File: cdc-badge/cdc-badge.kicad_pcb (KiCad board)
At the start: 4 copper layers, 85 x 110 mm, 158 parts, among them J1 USB_C, J2 JST S2B-PH-SM4-TB, J3 Conn_02x20_Odd_Even, J4 Conn_Grove, J5 Conn_02x03_Odd_Even, J6 Conn_01x06, J7 Conn_01x24, Q1 Si1308EDL, Q2 Si1308EDL, SW0 0, SW1 1, SW10 YES, SW11 NO, SW12 power on/reset, SW13 reset, SW14 flash/power off, SW15 MST-22D18G2 3J, SW16 MST-22D18G2 3J, SW2 2, SW3 3, SW4 4, SW5 5, SW6 6, SW7 7, SW8 8, SW9 9, U1 ESP32-S3-WROOM-1-N16R8, U2 TCA9535PWR, U3 TR01-C2P-T301, U5 TLV61070ADBVR, U6 BQ25895RTW, U8 TLV62569DBV

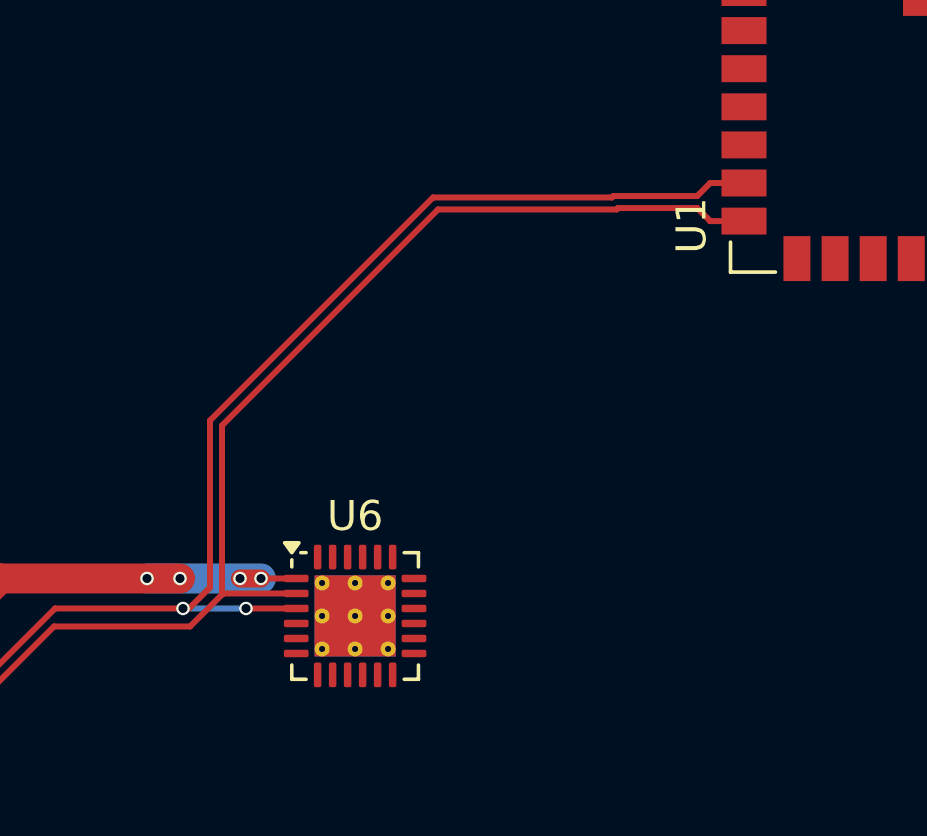
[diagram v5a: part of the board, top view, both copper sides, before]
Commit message: PCB: small changes in data line route and charging IC connections
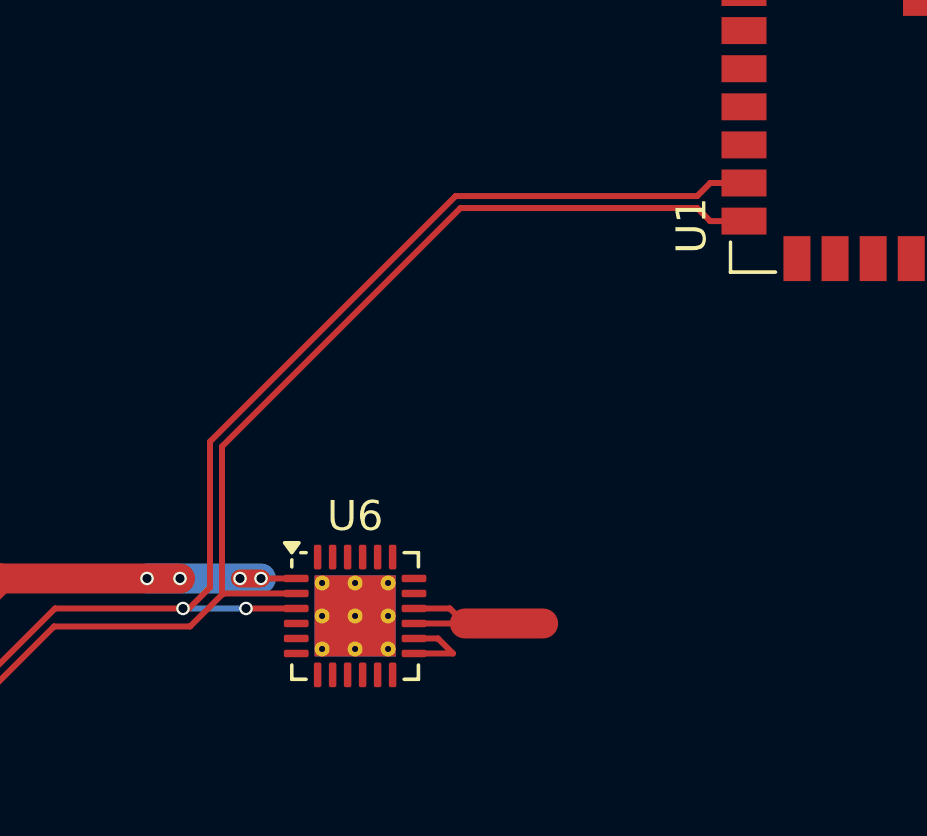
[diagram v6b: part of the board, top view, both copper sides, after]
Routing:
- net VSYS: track 0.00 -> 6.21 mm
- net Net-(J2-Pin_1): track 0.00 -> 2.81 mm
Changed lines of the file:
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@@
+	)
+	(segment
+		(start 96 92.3)
+		(end 96.8 92.3)
+		(width 0.2)
+		(layer "F.Cu")
+		(net 32)
+	)
+	(segment
+		(start 96 92.8)
+		(end 97.3 92.8)
+		(width 0.2)
+		(layer "F.Cu")
+		(net 32)
+	)
+	(segment
+		(start 96.8 92.3)
+		(end 97.3 92.8)
+		(width 0.2)
+		(layer "F.Cu")
+		(net 32)
+	)
+	(segment
+		(start 97.195 91.3)
+		(end 97.695 91.8)
+		(width 0.2)
+		(layer "F.Cu")
+		(net 34)
+	)
+	(segment
+		(start 97.695 91.8)
+		(end 100.305 91.8)
+		(width 1)
+		(layer "F.Cu")
+		(net 34)
+	)
+	(segment
+		(start 96 91.3)
+		(end 97.195 91.3)
+		(width 0.2)
+		(layer "F.Cu")
+		(net 34)
+	)
+	(segment
+		(start 97.695 91.8)
+		(end 96 91.8)
+		(width 0.2)
+		(layer "F.Cu")
+		(net 34)
 	)
 	(segment
@@
 	)
 	(segment
-		(start 96.634314 77.6)
-		(end 102.6 77.6)
-		(width 0.2)
-		(layer "F.Cu")
-		(net 69)
-	)
-	(segment
 		(start 61.105 104.75)
 		(end 60.8 104.445)
@@
 	)
 	(segment
+		(start 97.3875 77.5525)
+		(end 89.2 85.74)
+		(width 0.2)
+		(layer "F.Cu")
+		(net 69)
+	)
+	(segment
+		(start 107 77.1175)
+		(end 105.874999 77.1175)
+		(width 0.2)
+		(layer "F.Cu")
+		(net 69)
+	)
+	(segment
 		(start 60.8 104.445)
 		(end 60.8 104)
@@
 	(segment
 		(start 89.2 90.6)
-		(end 89.2 85.034314)
-		(width 0.2)
-		(layer "F.Cu")
-		(net 69)
-	)
-	(segment
-		(start 102.6475 77.5525)
-		(end 105.439999 77.5525)
-		(width 0.2)
-		(layer "F.Cu")
-		(net 69)
-	)
-	(segment
-		(start 105.439999 77.5525)
-		(end 105.874999 77.1175)
+		(end 88.5 91.3)
 		(width 0.2)
 		(layer "F.Cu")
@@
 	)
 	(segment
-		(start 88.3 91.3)
-		(end 88.5 91.3)
-		(width 0.2)
-		(layer "F.Cu")
-		(net 69)
-	)
-	(segment
 		(start 88.5 91.3)
-		(end 89.2 90.6)
+		(end 88.3 91.3)
+		(width 0.2)
+		(layer "F.Cu")
+		(net 69)
+	)
+	(segment
+		(start 105.439999 77.5525)
+		(end 97.3875 77.5525)
 		(width 0.2)
 		(layer "F.Cu")
@@
 	)
 	(segment
-		(start 102.6 77.6)
-		(end 102.6475 77.5525)
-		(width 0.2)
-		(layer "F.Cu")
-		(net 69)
-	)
-	(segment
 		(start 92.075 91.3)
 		(end 90.4 91.3)
@@
 	)
 	(segment
-		(start 105.874999 77.1175)
-		(end 107 77.1175)
-		(width 0.2)
-		(layer "F.Cu")
-		(net 69)
-	)
-	(segment
-		(start 89.2 85.034314)
-		(end 96.634314 77.6)
+		(start 89.2 85.74)
+		(end 89.2 90.6)
 		(width 0.2)
 		(layer "F.Cu")
@@
 		(net 69)
 	)
+	(segment
+		(start 105.874999 77.1175)
+		(end 105.439999 77.5525)
+		(width 0.2)
+		(layer "F.Cu")
+		(net 69)
+	)
 	(via
 		(at 90.4 91.3)
@@
 	)
 	(segment
+		(start 62.645 105.25)
+		(end 63 104.895)
+		(width 0.2)
+		(layer "F.Cu")
+		(net 70)
+	)
+	(segment
+		(start 63 104.2)
+		(end 63.172 104.372)
+		(width 0.2)
+		(layer "F.Cu")
+		(net 70)
+	)
+	(segment
+		(start 61.875 105.25)
+		(end 62.645 105.25)
+		(width 0.2)
+		(layer "F.Cu")
+		(net 70)
+	)
+	(segment
+		(start 63.172 104.372)
+		(end 71.528 104.372)
+		(width 0.2)
+		(layer "F.Cu")
+		(net 70)
+	)
+	(segment
+		(start 105.439999 77.9525)
+		(end 97.5475 77.9525)
+		(width 0.2)
+		(layer "F.Cu")
+		(net 70)
+	)
+	(segment
+		(start 62.730001 104.25)
+		(end 61.875 104.25)
+		(width 0.2)
+		(layer "F.Cu")
+		(net 70)
+	)
+	(segment
+		(start 63 104.2)
+		(end 62.780001 104.2)
+		(width 0.2)
+		(layer "F.Cu")
+		(net 70)
+	)
+	(segment
+		(start 89.6 90.837248)
+		(end 89.637248 90.8)
+		(width 0.2)
+		(layer "F.Cu")
+		(net 70)
+	)
+	(segment
+		(start 88.537248 91.9)
+		(end 84 91.9)
+		(width 0.2)
+		(layer "F.Cu")
+		(net 70)
+	)
+	(segment
+		(start 105.874999 78.3875)
+		(end 105.439999 77.9525)
+		(width 0.2)
+		(layer "F.Cu")
+		(net 70)
+	)
+	(segment
+		(start 63 104.895)
+		(end 63 104.2)
+		(width 0.2)
+		(layer "F.Cu")
+		(net 70)
+	)
+	(segment
+		(start 89.637248 90.8)
+		(end 92.075 90.8)
+		(width 0.2)
+		(layer "F.Cu")
+		(net 70)
+	)
+	(segment
+		(start 97.5475 77.9525)
+		(end 89.6 85.9)
+		(width 0.2)
+		(layer "F.Cu")
+		(net 70)
+	)
+	(segment
+		(start 84 91.9)
+		(end 71.55 104.35)
+		(width 0.2)
+		(layer "F.Cu")
+		(net 70)
+	)
+	(segment
 		(start 107 78.3875)
 		(end 105.874999 78.3875)
@@
 	)
 	(segment
-		(start 62.645 105.25)
-		(end 63 104.895)
-		(width 0.2)
-		(layer "F.Cu")
-		(net 70)
-	)
-	(segment
-		(start 63 104.2)
-		(end 63.172 104.372)
-		(width 0.2)
-		(layer "F.Cu")
-		(net 70)
-	)
-	(segment
-		(start 61.875 105.25)
-		(end 62.645 105.25)
-		(width 0.2)
-		(layer "F.Cu")
-		(net 70)
-	)
-	(segment
-		(start 63.172 104.372)
-		(end 71.528 104.372)
-		(width 0.2)
-		(layer "F.Cu")
-		(net 70)
-	)
-	(segment
-		(start 62.730001 104.25)
-		(end 61.875 104.25)
-		(width 0.2)
-		(layer "F.Cu")
-		(net 70)
-	)
-	(segment
-		(start 102.800572 77.9525)
-		(end 102.753072 78)
-		(width 0.2)
-		(layer "F.Cu")
-		(net 70)
-	)
-	(segment
-		(start 63 104.2)
-		(end 62.780001 104.2)
-		(width 0.2)
-		(layer "F.Cu")
-		(net 70)
-	)
-	(segment
-		(start 89.6 90.837248)
-		(end 89.637248 90.8)
-		(width 0.2)
-		(layer "F.Cu")
-		(net 70)
-	)
-	(segment
-		(start 88.537248 91.9)
-		(end 84 91.9)
-		(width 0.2)
-		(layer "F.Cu")
-		(net 70)
-	)
-	(segment
-		(start 63 104.895)
-		(end 63 104.2)
-		(width 0.2)
-		(layer "F.Cu")
-		(net 70)
-	)
-	(segment
-		(start 89.637248 90.8)
-		(end 92.075 90.8)
-		(width 0.2)
-		(layer "F.Cu")
-		(net 70)
-	)
-	(segment
-		(start 105.874999 78.3875)
-		(end 105.439999 77.9525)
-		(width 0.2)
-		(layer "F.Cu")
-		(net 70)
-	)
-	(segment
-		(start 96.8 78)
-		(end 89.6 85.2)
-		(width 0.2)
-		(layer "F.Cu")
-		(net 70)
-	)
-	(segment
-		(start 84 91.9)
-		(end 71.55 104.35)
-		(width 0.2)
-		(layer "F.Cu")
-		(net 70)
-	)
-	(segment
-		(start 105.439999 77.9525)
-		(end 102.800572 77.9525)
-		(width 0.2)
-		(layer "F.Cu")
-		(net 70)
-	)
-	(segment
 		(start 62.780001 104.2)
 		(end 62.730001 104.25)
@@
 	)
 	(segment
-		(start 89.6 85.2)
+		(start 89.6 85.9)
 		(end 89.6 90.837248)
 		(width 0.2)
 		(layer "F.Cu")
-		(net 70)
-	)
-	(segment
-		(start 102.753072 78)
-		(end 96.8 78)
-		(width 0.2)
-		(layer "F.Cu")

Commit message: PCB: 5V boostconverter draft layout
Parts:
- moved R13 109.4 mm to (59.7, 97.6), turned to 180 degrees
- moved C36 103.6 mm to (100.7, 92.5), turned to -90 degrees
- moved LED1 103.5 mm to (59.6, 95.8)
- moved C37 100.3 mm to (98.7, 92.5), turned to -90 degrees
- moved C35 96.3 mm to (94.9, 87.5), turned to 180 degrees
- moved L1 64.2 mm to (99.2, 88.5)
- moved R18 50.6 mm to (245.1, 116.0)
- moved C6 21.6 mm to (184.1, 102.8), turned to 90 degrees
- moved C14 19.4 mm to (185.6, 84.0)
- moved C7 18.7 mm to (188.2, 105.0), turned to 90 degrees
- moved C8 13.3 mm to (192.2, 105.0), turned to 90 degrees
- moved R44 12.3 mm to (187.9, 108.2), turned to -90 degrees
- moved U5 11.4 mm to (185.0, 106.3)
- moved C9 10.6 mm to (190.2, 105.0), turned to 90 degrees
- moved C49 7.21 mm to (189.5, 108.2), turned to -90 degrees
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- renumbered D1 to LED1
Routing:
- net /REGN: track 0.00 -> 37.8 mm, vias 0 -> 2
- net Net-(U6-STAT): track 0.00 -> 34.1 mm, vias 0 -> 2
- net VSYS: track 6.21 -> 31.9 mm
- net GND: track 10.8 -> 22.5 mm, vias 20 -> 32
- net Net-(C35-Pad1): track 0.00 -> 5.74 mm
- net Net-(U5-SW): track 0.00 -> 3.52 mm
- net Net-(J2-Pin_1): track 2.81 -> 5.42 mm
- net Net-(U6-BTST): track 0.00 -> 2.25 mm
- net Net-(D1-K): track 0.00 -> 1.81 mm
- net Net-(U5-V_{FB}): track 0.00 -> 1.52 mm

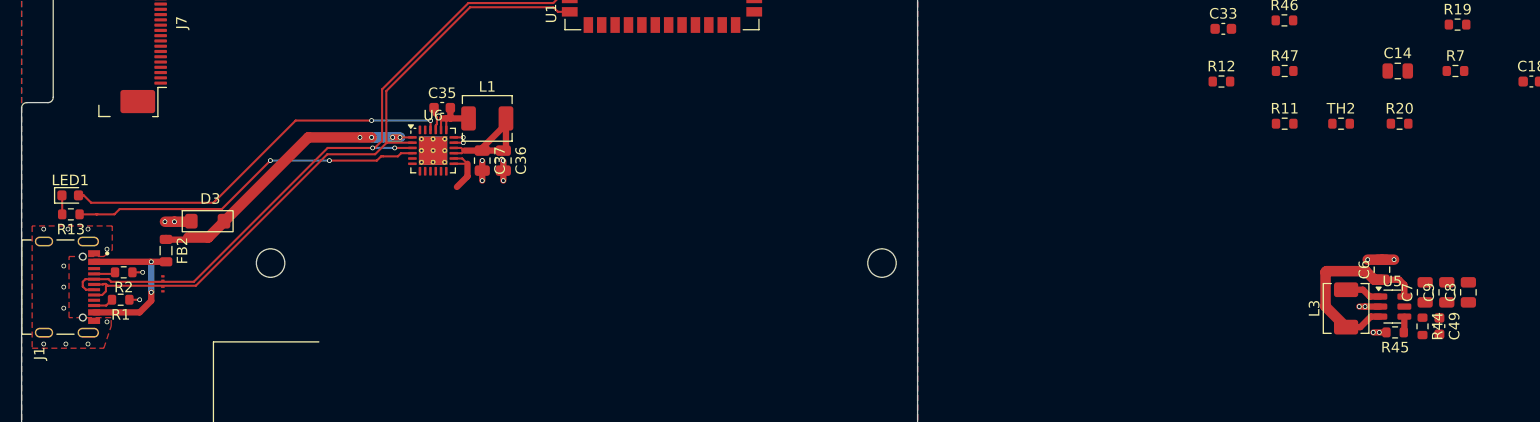
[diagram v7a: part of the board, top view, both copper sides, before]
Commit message: pcb: layout boost converter, review charging IC zones
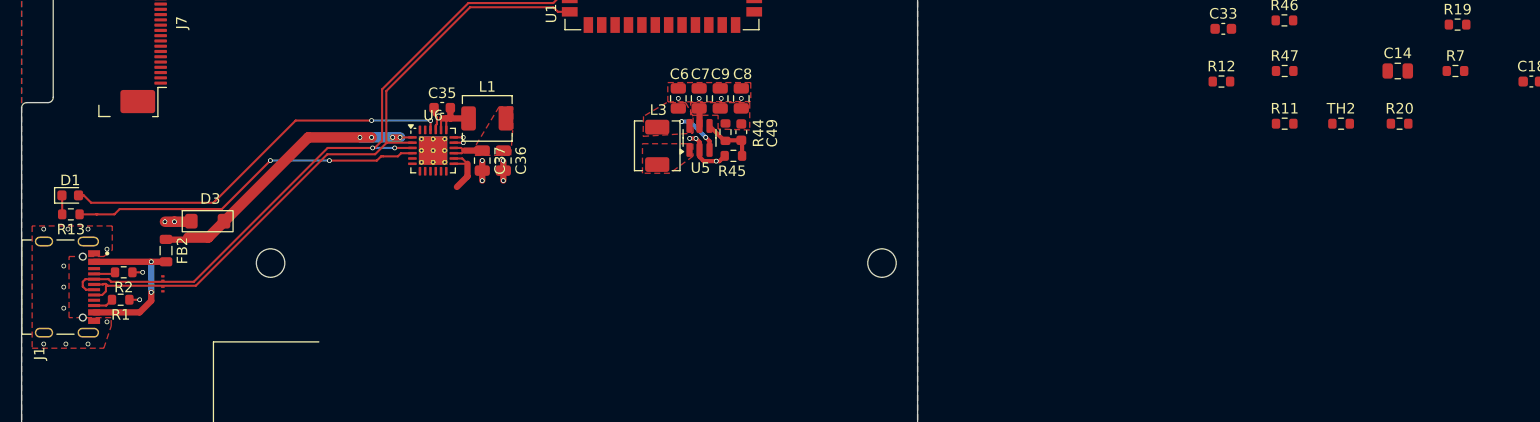
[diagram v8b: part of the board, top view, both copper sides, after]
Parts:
- moved C8 71.4 mm to (123.3, 86.6)
- moved C9 71.3 mm to (121.3, 86.6)
- moved C7 71.3 mm to (119.3, 86.6)
- moved C49 68.7 mm to (123.3, 89.8)
- moved C6 68.7 mm to (117.3, 86.6)
- moved R44 68.6 mm to (121.8, 89.8)
- moved U5 67.6 mm to (119.3, 90.3), turned to 90 degrees
- moved L3 67.1 mm to (115.3, 91.1), turned to -90 degrees
- moved R45 65.0 mm to (122.5, 92.0)
- renumbered LED1 to D1
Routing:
- net VSYS: track 31.9 -> 8.76 mm, vias 0 -> 2
- net Net-(U5-V_{FB}): track 1.52 -> 5.08 mm
- net Net-(U5-SW): track 3.52 -> 0.00 mm
- net +5V: track 0.00 -> 1.68 mm
- net GND: track 22.5 -> 22.0 mm, vias 32 -> 33
- added copper zone on F.Cu, net +5V
- added copper zone on F.Cu, net Net-(U5-SW)
- added copper zone on F.Cu, net VSYS
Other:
- board text removed: "5V"
